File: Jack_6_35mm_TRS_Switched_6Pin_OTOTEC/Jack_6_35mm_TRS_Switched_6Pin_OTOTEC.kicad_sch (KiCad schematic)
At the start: 0 parts

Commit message: feat: finish first working jack breakout PCB
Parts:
- added J1: NMJ6HCD2, OTOTEC:Jack_6.35mm_OTOTEC_TRS_Switched_6Pin, symbol Connector_Audio:NMJ6HCD2
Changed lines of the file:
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@@
 	(generator_version "10.0")
 	(paper "A4")
+	(symbol
+		(lib_id "Connector_Audio:NMJ6HCD2")
+		(at 55.88 48.26 0)
+		(unit 1)
+		(body_style 1)
+		(exclude_from_sim no)
+		(in_bom yes)
+		(on_board yes)
+		(in_pos_files yes)
+		(dnp no)
+		(fields_autoplaced yes)
+		(property "Reference" "J1"
+			(at 53.975 36.83 0)
+			(show_name no)
+			(do_not_autoplace no)
+			(effects
+				(font
+					(size 1.27 1.27)
+				)
+			)
+		)
+		(property "Value" "NMJ6HCD2"
+			(at 53.975 39.37 0)
+			(show_name no)
+			(do_not_autoplace no)
+			(effects
+				(font
+					(size 1.27 1.27)
+				)
+			)
+		)
+		(property "Footprint" "OTOTEC:Jack_6.35mm_OTOTEC_TRS_Switched_6Pin"
+			(at 55.88 48.26 0)
+			(hide yes)
+			(show_name no)
+			(do_not_autoplace no)
+			(effects
+				(font
+					(size 1.27 1.27)
+				)
+			)
+		)
+		(property "Datasheet" "https://www.neutrik.com/en/product/nmj6hcd2"
+			(at 55.88 48.26 0)
+			(hide yes)
+			(show_name no)
+			(do_not_autoplace no)
+			(effects
+				(font
+					(size 1.27 1.27)
+				)
+			)
+		)
+		(property "Description" "M Series, 6.35mm (1/4in) stereo jack, switched, with chrome ferrule and straight PCB pins"
+			(at 55.88 48.26 0)
+			(hide yes)
+			(show_name no)
+			(do_not_autoplace no)
+			(effects
+				(font
+					(size 1.27 1.27)
+				)
+			)
+		)
+		(pin "R"
+		)
+		(pin "RN"
+		)
+		(pin "S"
+		)
+		(pin "SN"
+		)
+		(pin "T"
+		)
+		(pin "TN"
+		)
+		(instances
+			(project "Jack_6_35mm_TRS_Switched_6Pin_OTOTEC"
+				(path "/f8591ae7-1241-4b97-b2f8-4e0614dca332"
+					(reference "J1")
+					(unit 1)
+				)
+			)
+		)
+	)
 	(sheet_instances
 		(path "/"

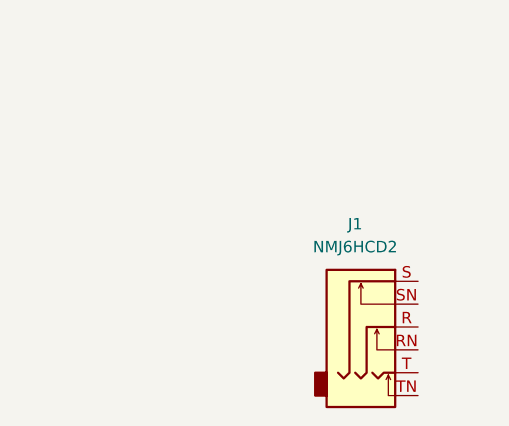
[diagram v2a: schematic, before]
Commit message: feat: improve breadboard connectivity
- Added 3-pin headers for easier breadboard connection
- Added proper schematic connections and net routing
- Improved PCB layout with rounded corners
- Added project metadata and schematic title
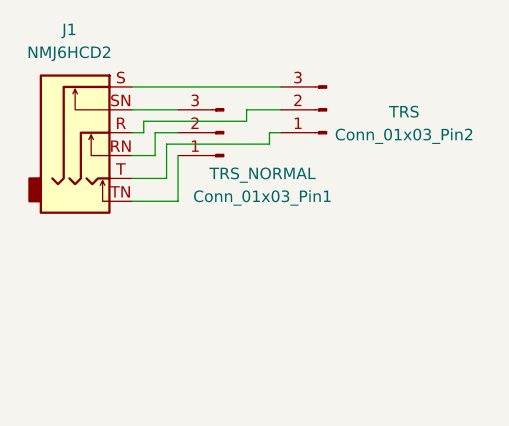
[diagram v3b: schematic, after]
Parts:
- added Conn_01x03_Pin1: TRS_NORMAL, Connector_PinHeader_2.54mm:PinHeader_1x03_P2.54mm_Vertical, symbol Connector:Conn_01x03_Pin
- added Conn_01x03_Pin2: TRS, Connector_PinHeader_2.54mm:PinHeader_1x03_P2.54mm_Vertical, symbol Connector:Conn_01x03_Pin
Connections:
- net at J1.R: now also Conn_01x03_Pin2.2 (Pin_2)
- net at J1.RN: now also Conn_01x03_Pin1.2 (Pin_2)
- net at J1.S: now also Conn_01x03_Pin2.3 (Pin_3)
- net at J1.SN: now also Conn_01x03_Pin1.3 (Pin_3)
- net at J1.T: now also Conn_01x03_Pin2.1 (Pin_1)
- net at J1.TN: now also Conn_01x03_Pin1.1 (Pin_1)
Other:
- company: (none) -> adb-dev.tech
- title: (none) -> 6.35 mm Switched TRS Jack Breadboard Adapter
- moved on the sheet: J1

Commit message: feat: finalize TRS breadboard adapter Rev 1
- Increase signal trace width to 0.8 mm
- Add TRS and switched-contact pin labels
- Add jack orientation marker
- Add artwork and silkscreen details;
- Add AJDB logo footprint
- Add project identification and repository information
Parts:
- Conn_01x03_Pin1, Conn_01x03_Pin2: footprint Connector_PinHeader_2.54mm:PinHeader_1x03_P2.54mm_Vertical -> OTOTEC:PinHeader_1x03_P2.54mm_Vertical
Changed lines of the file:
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@@
 			)
 		)
-		(property "Footprint" "Connector_PinHeader_2.54mm:PinHeader_1x03_P2.54mm_Vertical"
+		(property "Footprint" "OTOTEC:PinHeader_1x03_P2.54mm_Vertical"
 			(at 50.8 24.13 0)
 			(hide yes)
@@
 			)
 		)
-		(property "Footprint" "Connector_PinHeader_2.54mm:PinHeader_1x03_P2.54mm_Vertical"
+		(property "Footprint" "OTOTEC:PinHeader_1x03_P2.54mm_Vertical"
 			(at 39.37 26.67 0)
 			(hide yes)
